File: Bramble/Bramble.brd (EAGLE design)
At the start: 84.8 x 55.9 mm, 10 parts, among them J1 614004134726, J2 614004134726, J3 614004134726, J4 614004134726, J5 614004134726, J6 614004134726, J7 614004134726, J8 614004134726, X1 MKDSN1,5/4-5,08

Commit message: Added labels
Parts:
- renumbered J1 to PWR1, J2 to PWR2, J3 to PWR3, J4 to PWR4, J5 to PWR8, J6 to PWR7, J7 to PWR6, J8 to PWR5, JP1 to FAN_PWR, X1 to PWR_IN
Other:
- board text added: "5V"

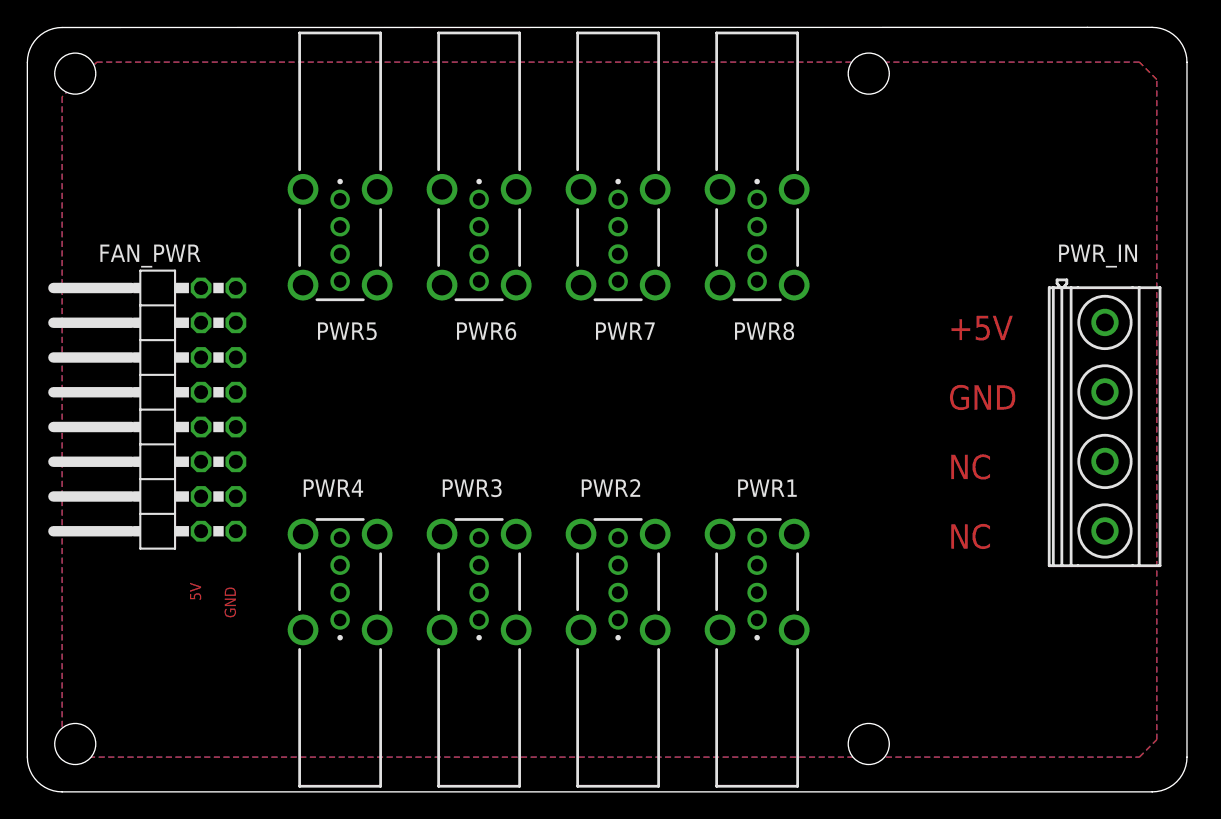
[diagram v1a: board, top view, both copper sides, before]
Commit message: Capacitors among USB connectors
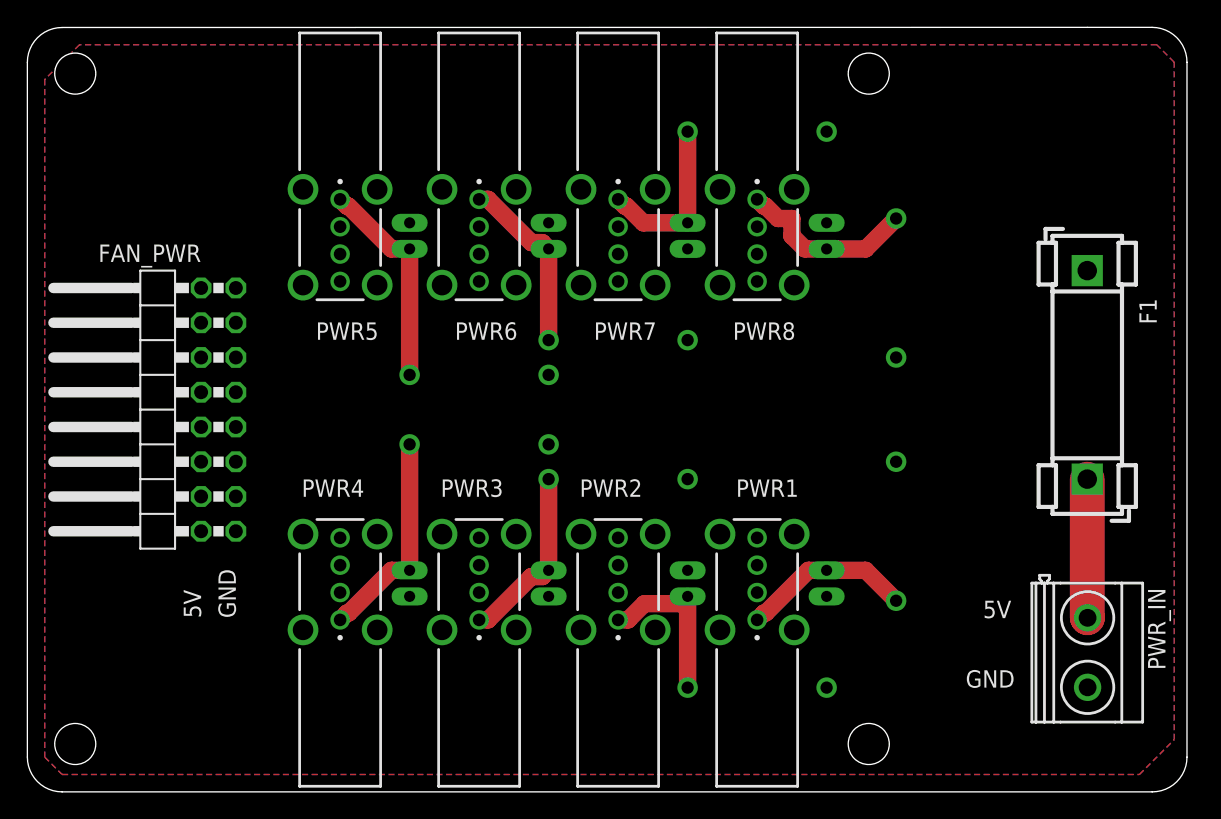
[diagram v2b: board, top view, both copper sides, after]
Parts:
- added C1, C2, C3, C4, C5, C6, C7, C8: 100uF, cap-master:ENP-020-050
- added F1: FUSEBLANK_5X20MM, fuse:FUSE_HOLDER_5X20MM
- added L1, L2, L3, L4, L5, L6, L7, L8: BL01RN1A, inductors:BL01RN1A
- PWR_IN: value MKDSN1,5/4-5,08 -> MKDSN1,5/2-5,08; device con-phoenix-508:MKDSN1,5/4-5,08 -> con-phoenix-508:MKDSN1,5/2-5,08
- moved PWR_IN 16.6 mm to (77.5, 10.2)
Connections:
- new net N$1: C1.1, L1.1, PWR1.1
- new net N$2: C2.1, L2.1, PWR2.1
- new net N$3: C4.1, L4.1, PWR4.1
- new net N$4: C3.1, L3.1, PWR3.1
- new net N$5: C5.1, L5.1, PWR5.1
- new net N$6: C6.1, L6.1, PWR6.1
- new net N$7: C7.1, L7.1, PWR7.1
- new net N$8: C8.1, L8.1, PWR8.1
- new net N$9: F1.2, PWR_IN.1
- net 5V: now also L1.2, L2.2, L3.2, L4.2, L5.2, L6.2, L7.2, L8.2; no longer PWR1.1, PWR2.1, PWR3.1, PWR4.1, PWR5.1, PWR6.1, PWR7.1, PWR8.1, PWR_IN.1
- net GND: now also C1.2, C2.2, C3.2, C4.2, C5.2, C6.2, C7.2, C8.2
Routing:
- net N$5: track 0.00 -> 15.8 mm
- net N$3: track 0.00 -> 15.8 mm
- net N$8: track 0.00 -> 13.3 mm
- net N$4: track 0.00 -> 13.2 mm
- net N$6: track 0.00 -> 13.2 mm
- net N$1: track 0.00 -> 12.6 mm
- net N$7: track 0.00 -> 12.5 mm
- net N$2: track 0.00 -> 12.5 mm
- net N$9: track 0.00 -> 10.1 mm
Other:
- board text removed: "+5V"
- board text removed: "NC"

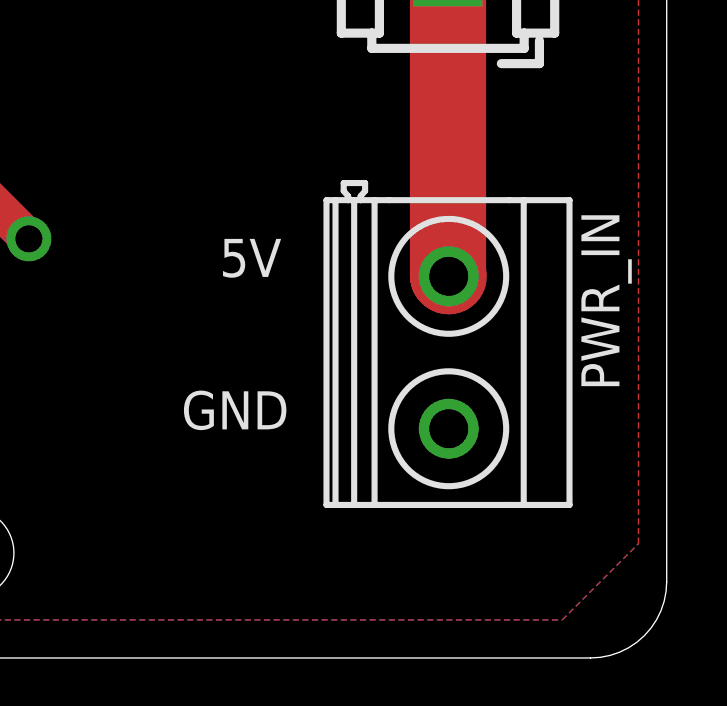
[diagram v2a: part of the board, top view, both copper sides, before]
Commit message: Rotated PWR IN connector
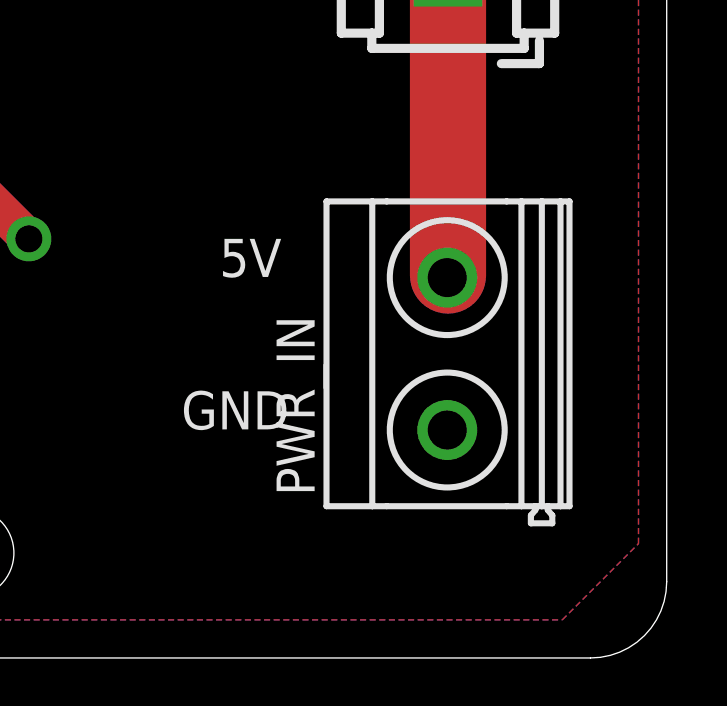
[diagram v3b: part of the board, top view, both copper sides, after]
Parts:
- turned PWR_IN to 90 degrees
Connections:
- net GND: now also PWR_IN.1; no longer PWR_IN.2
- net N$9: now also PWR_IN.2; no longer PWR_IN.1
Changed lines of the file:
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@@
 <attribute name="VALUE" x="62.23" y="41.5925" size="0.8128" layer="28" ratio="10" rot="MR270"/>
 </element>
-<element name="PWR_IN" library="con-phoenix-508" library_urn="urn:adsk.eagle:library:176" package="MKDSN1,5/2-5,08" package3d_urn="urn:adsk.eagle:package:9630/1" value="MKDSN1,5/2-5,08" x="77.47" y="10.16" smashed="yes" rot="R270">
-<attribute name="NAME" x="81.915" y="14.9111" size="1.27" layer="25" rot="R270"/>
-<attribute name="POPULARITY" value="14" x="77.47" y="10.16" size="1.778" layer="27" rot="R270" display="off"/>
+<element name="PWR_IN" library="con-phoenix-508" library_urn="urn:adsk.eagle:library:176" package="MKDSN1,5/2-5,08" package3d_urn="urn:adsk.eagle:package:9630/1" value="MKDSN1,5/2-5,08" x="77.47" y="10.16" smashed="yes" rot="R90">
+<attribute name="NAME" x="73.025" y="5.4089" size="1.27" layer="25" rot="R90"/>
+<attribute name="POPULARITY" value="14" x="77.47" y="10.16" size="1.778" layer="27" rot="R90" display="off"/>
 </element>
 </elements>
@@
 <contactref element="C7" pad="2"/>
 <contactref element="C8" pad="2"/>
-<contactref element="PWR_IN" pad="2"/>
+<contactref element="PWR_IN" pad="1"/>
 </signal>
 <signal name="N$1">
@@
 <signal name="N$9">
 <contactref element="F1" pad="2"/>
-<contactref element="PWR_IN" pad="1"/>
-<wire x1="77.495" y1="12.7211" x2="77.47" y2="12.7461" width="2.54" layer="1"/>
 <wire x1="77.47" y1="12.7461" x2="77.47" y2="22.86" width="2.54" layer="1"/>
+<contactref element="PWR_IN" pad="2"/>
+<wire x1="77.445" y1="12.6789" x2="77.47" y2="12.7461" width="0" layer="19" extent="1-1"/>
 </signal>
 </signals>

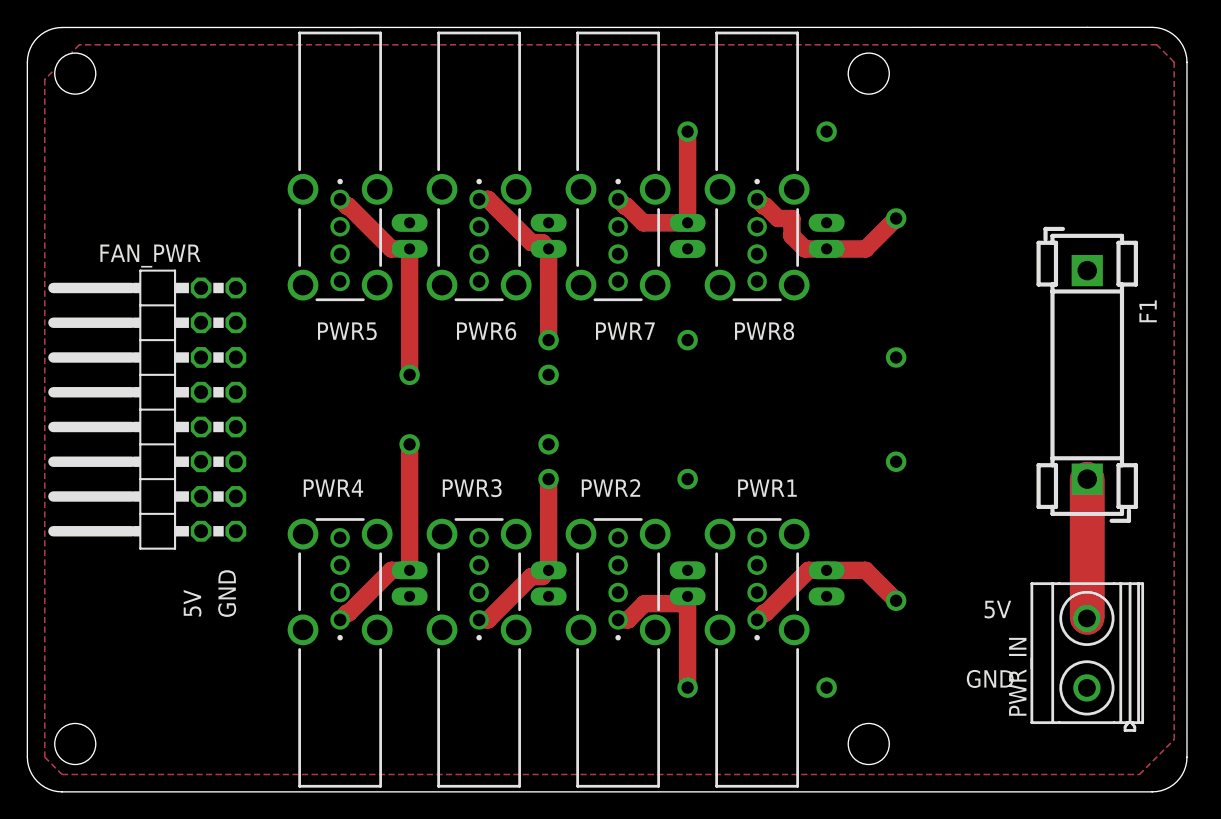
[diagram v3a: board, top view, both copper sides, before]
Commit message: Added capacitors for fans
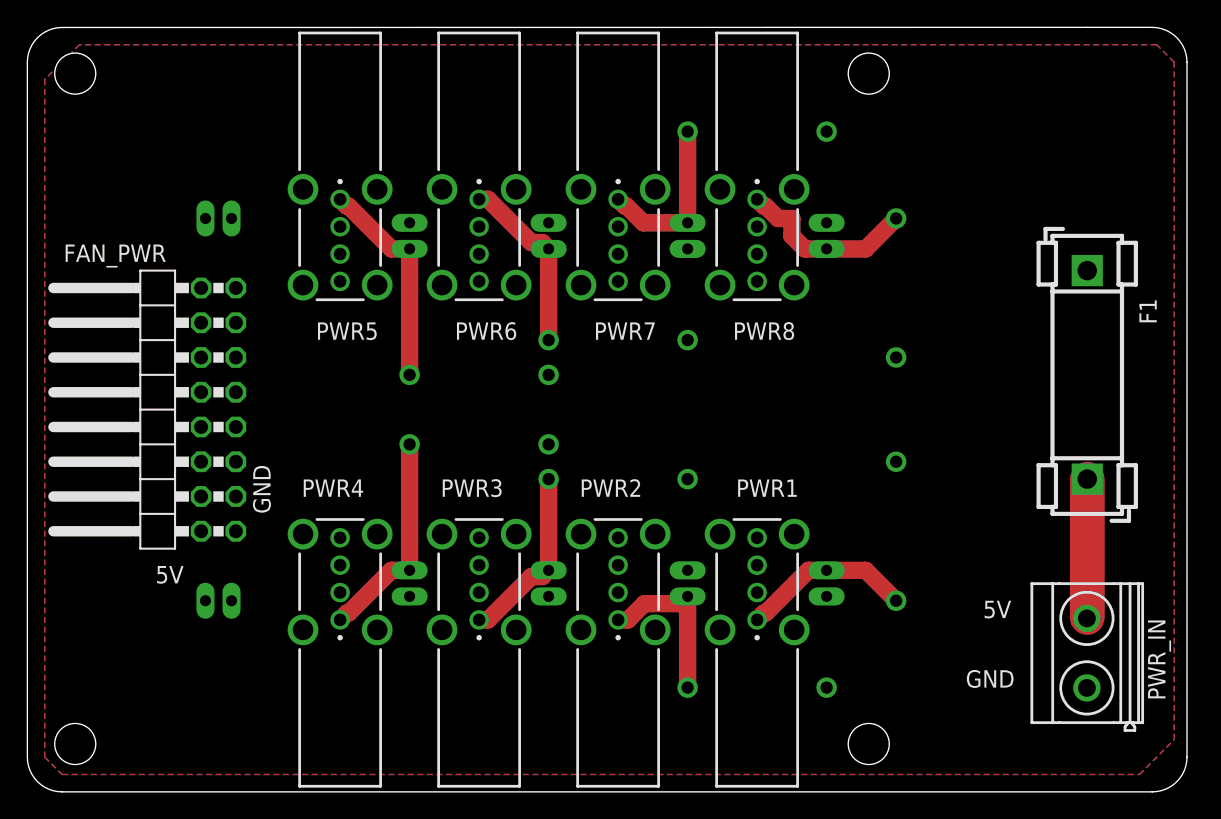
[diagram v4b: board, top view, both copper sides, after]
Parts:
- added C10, C9: 100uF, cap-master:ENP-020-050
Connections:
- net 5V: now also C10.1, C9.1
- net GND: now also C10.2, C9.2
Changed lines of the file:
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@@
 <drawing>
 <settings>
-<setting alwaysvectorfont="no"/>
+<setting alwaysvectorfont="yes"/>
 <setting verticaltext="up"/>
 </settings>
@@
 <text x="69.85" y="12.7" size="1.27" layer="25">5V</text>
 <text x="68.58" y="7.62" size="1.27" layer="25">GND</text>
-<text x="15.24" y="12.7" size="1.27" layer="25" rot="R90">GND</text>
-<text x="12.7" y="12.7" size="1.27" layer="25" rot="R90">5V</text>
+<text x="17.78" y="20.32" size="1.27" layer="25" rot="R90">GND</text>
+<text x="11.43" y="16.51" size="1.27" layer="25" rot="R180">5V</text>
 </plain>
 <attributes>
@@
 <attribute name="MANUFACTURER" value="" x="8.89" y="27.94" size="1.778" layer="27" rot="R90" display="off"/>
 <attribute name="MPN" value="" x="8.89" y="27.94" size="1.778" layer="27" rot="R90" display="off"/>
-<attribute name="NAME" x="12.7" y="40.005" size="1.27" layer="25" ratio="10" rot="R180"/>
+<attribute name="NAME" x="10.16" y="40.005" size="1.27" layer="25" ratio="10" rot="R180"/>
 <attribute name="OPERATING_TEMP" value="" x="8.89" y="27.94" size="1.778" layer="27" rot="R90" display="off"/>
 <attribute name="PART_STATUS" value="" x="8.89" y="27.94" size="1.778" layer="27" rot="R90" display="off"/>
@@
 </element>
 <element name="PWR_IN" library="con-phoenix-508" library_urn="urn:adsk.eagle:library:176" package="MKDSN1,5/2-5,08" package3d_urn="urn:adsk.eagle:package:9630/1" value="MKDSN1,5/2-5,08" x="77.47" y="10.16" smashed="yes" rot="R90">
-<attribute name="NAME" x="73.025" y="5.4089" size="1.27" layer="25" rot="R90"/>
+<attribute name="NAME" x="83.185" y="6.6789" size="1.27" layer="25" rot="R90"/>
 <attribute name="POPULARITY" value="14" x="77.47" y="10.16" size="1.778" layer="27" rot="R90" display="off"/>
+</element>
+<element name="C9" library="cap-master" package="ENP-020-050" value="100uF" x="13.97" y="41.91" smashed="yes" rot="MR0">
+<attribute name="NAME" x="11.1125" y="43.18" size="1.27" layer="26" ratio="14" rot="MR0"/>
+<attribute name="VALUE" x="11.1125" y="39.37" size="0.8128" layer="28" ratio="10" rot="MR0"/>
+</element>
+<element name="C10" library="cap-master" package="ENP-020-050" value="100uF" x="13.97" y="13.97" smashed="yes" rot="MR0">
+<attribute name="NAME" x="11.1125" y="15.24" size="1.27" layer="26" ratio="14" rot="MR0"/>
+<attribute name="VALUE" x="11.1125" y="11.43" size="0.8128" layer="28" ratio="10" rot="MR0"/>
 </element>
 </elements>
@@
 <contactref element="L6" pad="2"/>
 <contactref element="L5" pad="2"/>
+<contactref element="C10" pad="1"/>
+<contactref element="C9" pad="1"/>
 </signal>
 <signal name="GND">
@@
 <contactref element="C8" pad="2"/>
 <contactref element="PWR_IN" pad="1"/>
+<contactref element="C10" pad="2"/>
+<contactref element="C9" pad="2"/>
 </signal>
 <signal name="N$1">

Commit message: Reduction to 4 ports and SMD parts
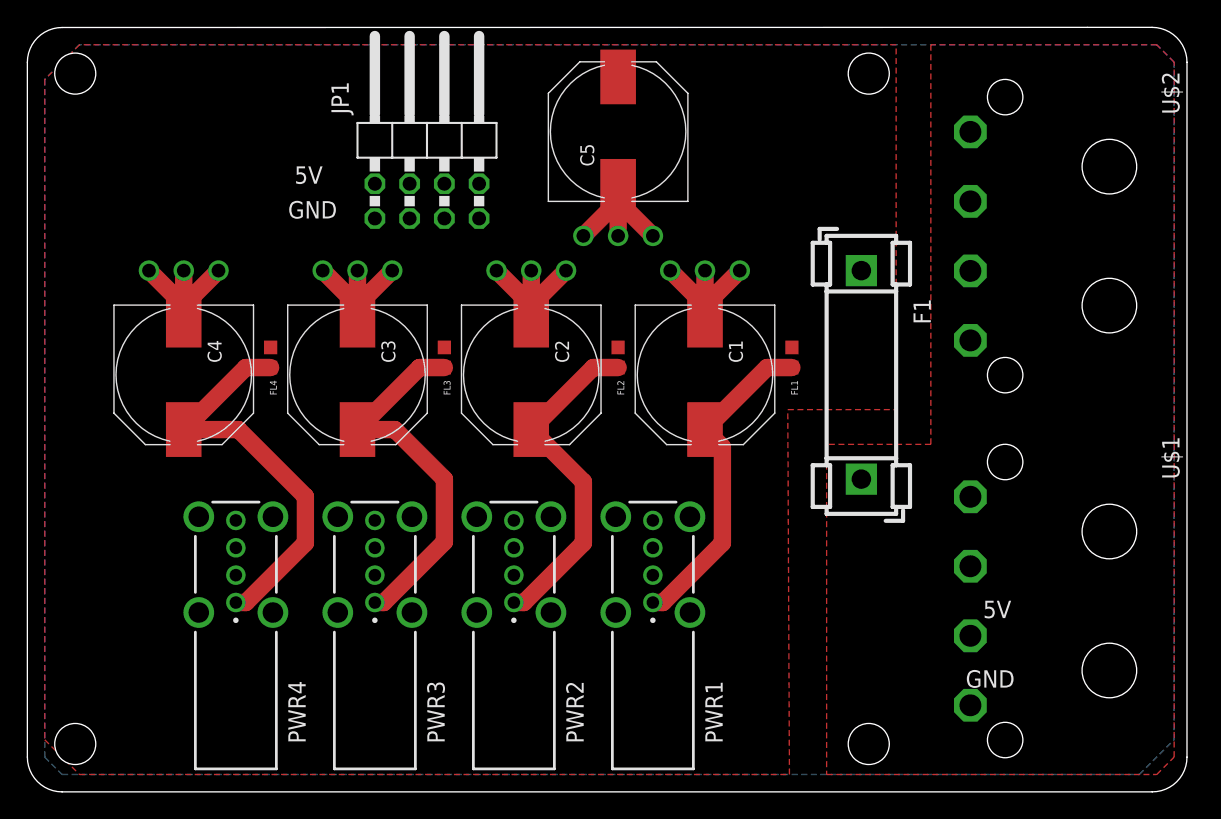
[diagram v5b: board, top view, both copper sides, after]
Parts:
- removed C10, C6, C7, C8, C9: 100uF, cap-master:ENP-020-050
- removed FAN_PWR: PINHD-2X8/90, Connector:2X08/90
- removed L1, L2, L3, L4, L5, L6, L7, L8: BL01RN1A, inductors:BL01RN1A
- removed PWR5, PWR6, PWR7, PWR8: 614004134726, Wurth_Connectors_WR-USB:614004134726
- removed PWR_IN: MKDSN1,5/2-5,08, con-phoenix-508:MKDSN1,5/2-5,08
- added FL1, FL2, FL3, FL4: BLM18PG121SH1D, BLM18PG121SH1D:BEADC1608X95N
- added JP1: PINHD-2X4/90, Connector:2X04/90
- added U$1, U$2: 15244441, 15244441:MOLEX_15244441
- C1, C2, C3, C4, C5: value 100uF -> CPOL-1010; device cap-master:ENP-020-050 -> cap-vishay-153clv:153CLV-1010
- moved C4 22.5 mm to (11.4, 30.5), flipped to the top
- moved C3 20.7 mm to (24.1, 30.5), flipped to the top
- moved C2 19.1 mm to (36.8, 30.5), flipped to the top, turned to 270 degrees
- moved C1 17.6 mm to (49.5, 30.5), flipped to the top
- moved C5 17.0 mm to (43.2, 48.3), flipped to the top
- moved F1 16.5 mm to (61.0, 38.1)
- moved PWR1 7.73 mm to (45.7, 11.4)
- moved PWR3 7.73 mm to (25.4, 11.4)
- moved PWR4 7.73 mm to (15.2, 11.4)
- moved PWR2 7.73 mm to (35.6, 11.4)
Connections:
- removed net N$5: C5.1, L5.1, PWR5.1
- removed net N$6: C6.1, L6.1, PWR6.1
- removed net N$7: C7.1, L7.1, PWR7.1
- removed net N$8: C8.1, L8.1, PWR8.1
- removed net N$9: F1.2, PWR_IN.2
- new net 5VIN: F1.2, U$1.1, U$2.1
- net 5V: now also C5.+, F1.1, FL1.2, FL2.2, FL3.2, FL4.2, JP1.2, JP1.4, JP1.6, JP1.8; no longer C10.1, C9.1, FAN_PWR.10, FAN_PWR.12, FAN_PWR.14, FAN_PWR.16, FAN_PWR.2, FAN_PWR.4, FAN_PWR.6, FAN_PWR.8, L1.2, L2.2, L3.2, L4.2, L5.2, L6.2, L7.2, L8.2
- net GND: now also C1.-, C2.-, C3.-, C4.-, C5.-, JP1.1, JP1.3, JP1.5, JP1.7, U$1.2, U$2.2; no longer C1.2, C10.2, C2.2, C3.2, C4.2, C5.2, C6.2, C7.2, C8.2, C9.2, FAN_PWR.1, FAN_PWR.11, FAN_PWR.13, FAN_PWR.15, FAN_PWR.3, FAN_PWR.5, FAN_PWR.7, FAN_PWR.9, PWR5.4, PWR5.S1, PWR5.S2, PWR5.S3, PWR5.S4, PWR6.4, PWR6.S1, PWR6.S2, PWR6.S3, PWR6.S4, PWR7.4, PWR7.S1, PWR7.S2, PWR7.S3, PWR7.S4, PWR8.4, PWR8.S1, PWR8.S2, PWR8.S3, PWR8.S4, PWR_IN.1
- net N$1: now also C1.+, FL1.1; no longer C1.1, L1.1
- net N$2: now also C2.+, FL2.1; no longer C2.1, L2.1
- net N$3: now also C4.+, FL4.1; no longer C4.1, L4.1
- net N$4: now also C3.+, FL3.1; no longer C3.1, L3.1
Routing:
- net GND: track 0.00 -> 58.5 mm, vias 0 -> 15
- net N$5: track 15.8 -> 0.00 mm
- net N$4: track 13.2 -> 27.6 mm
- net N$3: track 15.8 -> 29.4 mm
- net N$8: track 13.3 -> 0.00 mm
- net N$6: track 13.2 -> 0.00 mm
- net N$2: track 12.5 -> 25.0 mm
- net N$7: track 12.5 -> 0.00 mm
- net N$1: track 12.6 -> 23.9 mm
- net N$9: track 10.1 -> 0.00 mm
- added copper zone on layer 1, net 5VIN
